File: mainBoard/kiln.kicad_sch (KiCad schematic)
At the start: 0 parts

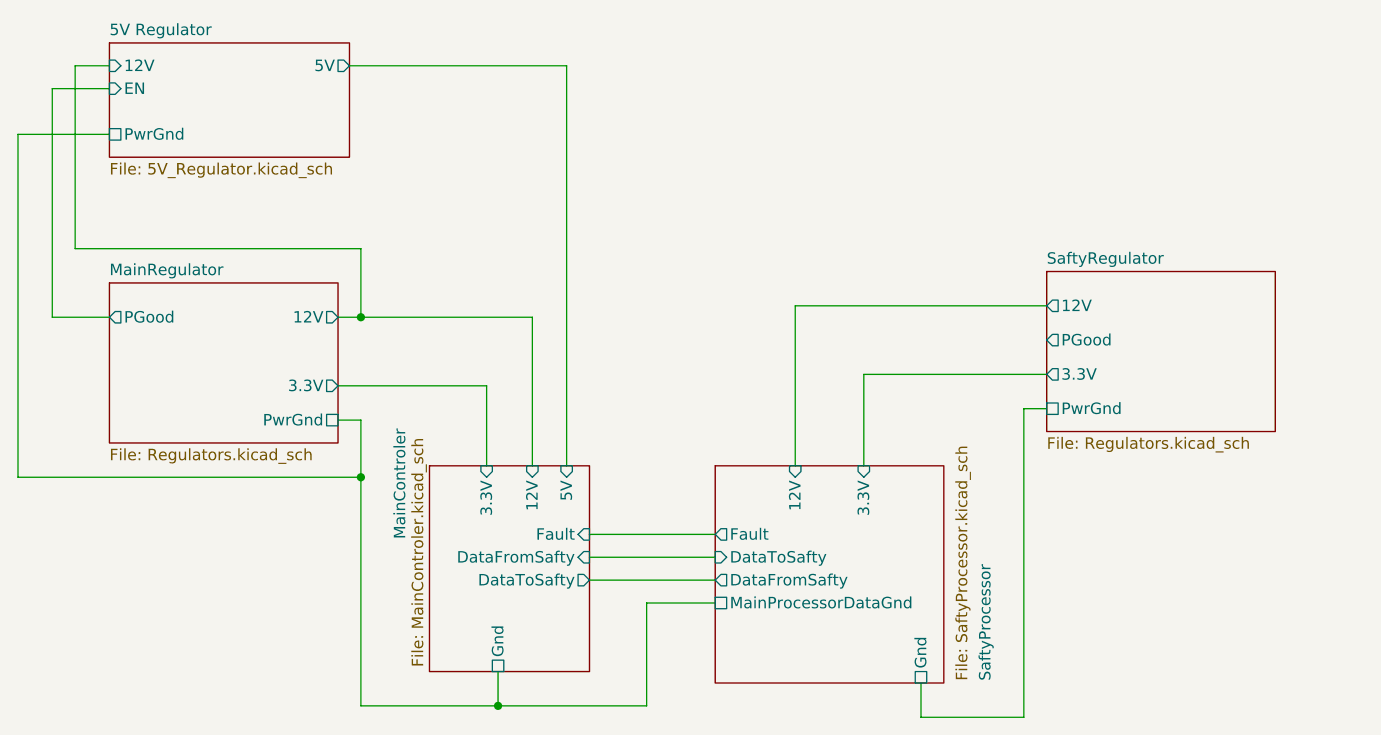
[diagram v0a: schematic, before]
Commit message: need to finish new regulators and run parts check on sch
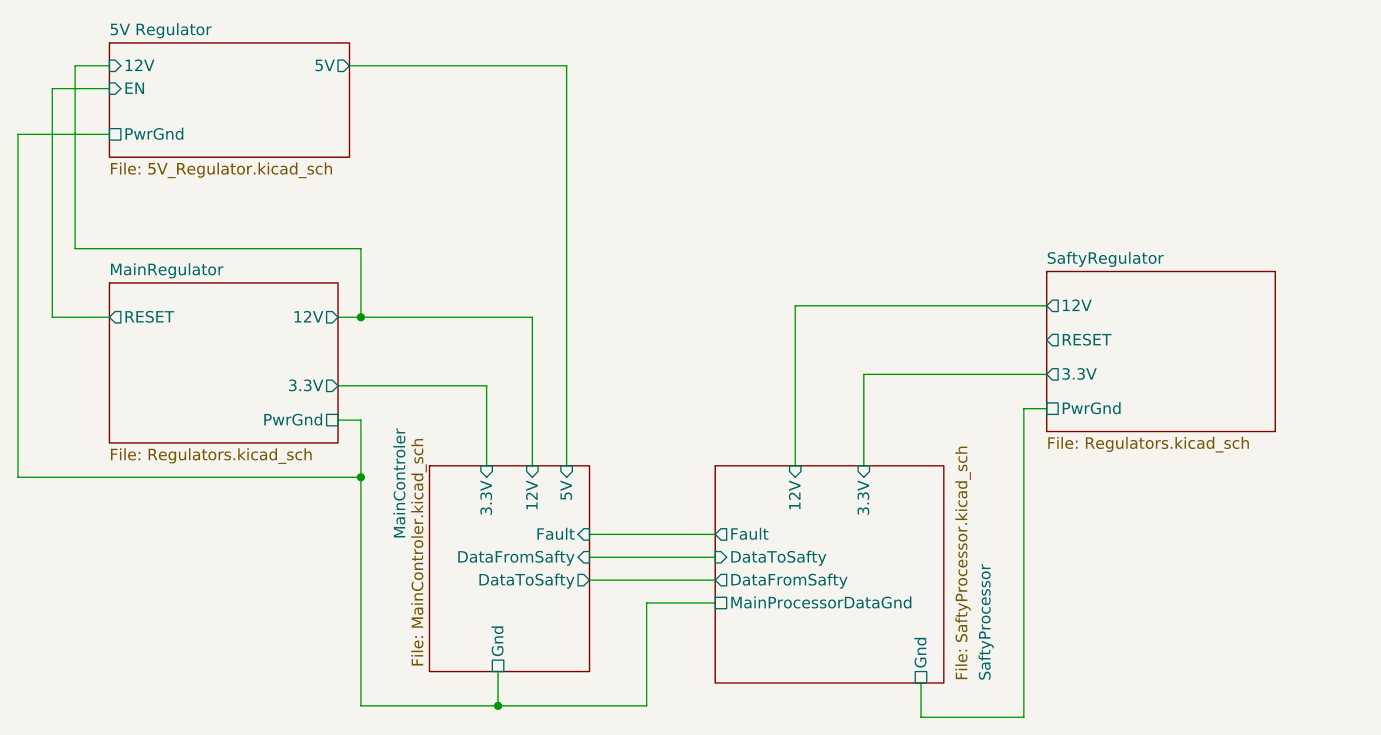
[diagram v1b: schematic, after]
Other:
- sheet MainRegulator ports: added RESET; removed PGood
- sheet SaftyRegulator ports: added RESET; removed PGood
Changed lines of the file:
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@@
 			)
 		)
-		(pin "PGood" output
+		(pin "RESET" output
 			(at 152.4 81.28 180)
 			(effects
@@
 			)
 		)
-		(pin "PGood" output
+		(pin "RESET" output
 			(at 48.26 78.74 180)
 			(effects

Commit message: almost done
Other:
- added sheet Safty 5V Regulator (5V_Regulator.kicad_sch)
- sheet SaftyProcessor ports: added 5V; removed none
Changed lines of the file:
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@@
+	)
+	(junction
+		(at 149.86 88.9)
+		(diameter 0)
+		(color 0 0 0 0)
+	)
+	(junction
+		(at 147.32 77.47)
+		(diameter 0)
+		(color 0 0 0 0)
 	)
 	(junction
@@
 	(wire
 		(pts
+			(xy 120.65 46.99) (xy 181.61 46.99)
+		)
+		(stroke
+			(width 0)
+			(type default)
+		)
+	)
+	(wire
+		(pts
 			(xy 91.44 118.11) (xy 91.44 121.92)
 		)
@@
 	(wire
 		(pts
+			(xy 181.61 46.99) (xy 181.61 54.61)
+		)
+		(stroke
+			(width 0)
+			(type default)
+		)
+	)
+	(wire
+		(pts
 			(xy 76.2 121.92) (xy 76.2 96.52)
 		)
@@
 	(wire
 		(pts
+			(xy 120.65 95.25) (xy 120.65 46.99)
+		)
+		(stroke
+			(width 0)
+			(type default)
+		)
+	)
+	(wire
+		(pts
 			(xy 132.08 85.09) (xy 132.08 95.25)
 		)
@@
 	(wire
 		(pts
+			(xy 149.86 62.23) (xy 153.67 62.23)
+		)
+		(stroke
+			(width 0)
+			(type default)
+		)
+	)
+	(wire
+		(pts
+			(xy 181.61 54.61) (xy 180.34 54.61)
+		)
+		(stroke
+			(width 0)
+			(type default)
+		)
+	)
+	(wire
+		(pts
 			(xy 107.95 110.49) (xy 107.95 121.92)
 		)
@@
 	(wire
 		(pts
+			(xy 149.86 88.9) (xy 149.86 62.23)
+		)
+		(stroke
+			(width 0)
+			(type default)
+		)
+	)
+	(wire
+		(pts
 			(xy 76.2 71.12) (xy 76.2 78.74)
 		)
@@
 	(wire
 		(pts
-			(xy 124.46 77.47) (xy 152.4 77.47)
+			(xy 124.46 77.47) (xy 147.32 77.47)
 		)
 		(stroke
@@
 	(wire
 		(pts
+			(xy 144.78 81.28) (xy 144.78 57.15)
+		)
+		(stroke
+			(width 0)
+			(type default)
+		)
+	)
+	(wire
+		(pts
 			(xy 138.43 123.19) (xy 149.86 123.19)
 		)
@@
 	(wire
 		(pts
+			(xy 147.32 54.61) (xy 153.67 54.61)
+		)
+		(stroke
+			(width 0)
+			(type default)
+		)
+	)
+	(wire
+		(pts
 			(xy 41.91 53.34) (xy 48.26 53.34)
 		)
@@
 	(wire
 		(pts
+			(xy 144.78 57.15) (xy 153.67 57.15)
+		)
+		(stroke
+			(width 0)
+			(type default)
+		)
+	)
+	(wire
+		(pts
 			(xy 76.2 90.17) (xy 73.66 90.17)
 		)
@@
 	(wire
 		(pts
+			(xy 152.4 81.28) (xy 144.78 81.28)
+		)
+		(stroke
+			(width 0)
+			(type default)
+		)
+	)
+	(wire
+		(pts
+			(xy 147.32 77.47) (xy 147.32 54.61)
+		)
+		(stroke
+			(width 0)
+			(type default)
+		)
+	)
+	(wire
+		(pts
 			(xy 149.86 123.19) (xy 149.86 88.9)
 		)
@@
 		(pts
 			(xy 41.91 78.74) (xy 41.91 53.34)
+		)
+		(stroke
+			(width 0)
+			(type default)
+		)
+	)
+	(wire
+		(pts
+			(xy 147.32 77.47) (xy 152.4 77.47)
 		)
 		(stroke
@@
 	)
 	(sheet
+		(at 153.67 52.07)
+		(size 26.67 12.7)
+		(exclude_from_sim no)
+		(in_bom yes)
+		(on_board yes)
+		(dnp no)
+		(fields_autoplaced yes)
+		(stroke
+			(width 0.1524)
+			(type solid)
+		)
+		(fill
+			(color 0 0 0 0)
+		)
+		(property "Sheetname" "Safty 5V Regulator"
+			(at 153.67 51.3584 0)
+			(show_name no)
+			(do_not_autoplace no)
+			(effects
+				(font
+					(size 1.27 1.27)
+				)
+				(justify left bottom)
+			)
+		)
+		(property "Sheetfile" "5V_Regulator.kicad_sch"
+			(at 153.67 65.3546 0)
+			(show_name no)
+			(do_not_autoplace no)
+			(effects
+				(font
+					(size 1.27 1.27)
+				)
+				(justify left top)
+			)
+		)
+		(pin "5V" output
+			(at 180.34 54.61 0)
+			(effects
+				(font
+					(size 1.27 1.27)
+				)
+				(justify right)
+			)
+		)
+		(pin "12V" input
+			(at 153.67 54.61 180)
+			(effects
+				(font
+					(size 1.27 1.27)
+				)
+				(justify left)
+			)
+		)
+		(pin "EN" input
+			(at 153.67 57.15 180)
+			(effects
+				(font
+					(size 1.27 1.27)
+				)
+				(justify left)
+			)
+		)
+		(pin "PwrGnd" passive
+			(at 153.67 62.23 180)
+			(effects
+				(font
+					(size 1.27 1.27)
+				)
+				(justify left)
+			)
+		)
+		(instances
+			(project "kiln"
+				(path "/e9c1836b-d16f-494a-819b-41549a786e18"
+					(page "7")
+				)
+			)
+		)
+	)
+	(sheet
 		(at 48.26 74.93)
 		(size 25.4 17.78)
@@
 			)
 		)
+		(pin "5V" input
+			(at 120.65 95.25 90)
+			(effects
+				(font
+					(size 1.27 1.27)
+				)
+				(justify right)
+			)
+		)

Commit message: Update Board. removed power sequencing of 5v because it violated the voltage range of the power supply reset pin
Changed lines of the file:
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@@
-	(wire
-		(pts
-			(xy 48.26 78.74) (xy 41.91 78.74)
-		)
-		(stroke
-			(width 0)
-			(type default)
-		)
-	)
 	(wire
 		(pts
@@
 	(wire
 		(pts
-			(xy 144.78 81.28) (xy 144.78 57.15)
-		)
-		(stroke
-			(width 0)
-			(type default)
-		)
-	)
-	(wire
-		(pts
 			(xy 138.43 123.19) (xy 149.86 123.19)
 		)
@@
 	(wire
 		(pts
-			(xy 41.91 53.34) (xy 48.26 53.34)
-		)
-		(stroke
-			(width 0)
-			(type default)
-		)
-	)
-	(wire
-		(pts
 			(xy 99.06 50.8) (xy 74.93 50.8)
 		)
@@
 	(wire
 		(pts
-			(xy 144.78 57.15) (xy 153.67 57.15)
-		)
-		(stroke
-			(width 0)
-			(type default)
-		)
-	)
-	(wire
-		(pts
 			(xy 76.2 90.17) (xy 73.66 90.17)
 		)
@@
 	(wire
 		(pts
-			(xy 152.4 81.28) (xy 144.78 81.28)
-		)
-		(stroke
-			(width 0)
-			(type default)
-		)
-	)
-	(wire
-		(pts
 			(xy 147.32 77.47) (xy 147.32 54.61)
 		)
@@
 		)
 		(stroke
-			(width 0)
-			(type default)
-		)
-	)
-	(wire
-		(pts
-			(xy 41.91 78.74) (xy 41.91 53.34)
-		)
-		(stroke
